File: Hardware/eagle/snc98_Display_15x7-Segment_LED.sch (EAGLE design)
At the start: 71 parts, among them M10 IRLML6402, M11 IRLML6402, M4 IRLML6402, M5 IRLML6402, M6 IRLML6402, M7 IRLML6402, M8 IRLML6402, M9 IRLML6402, X1 MICROMATCH-12, X2 MICROMATCH-14, X3 MICROMATCH-12, X4 MICROMATCH-14

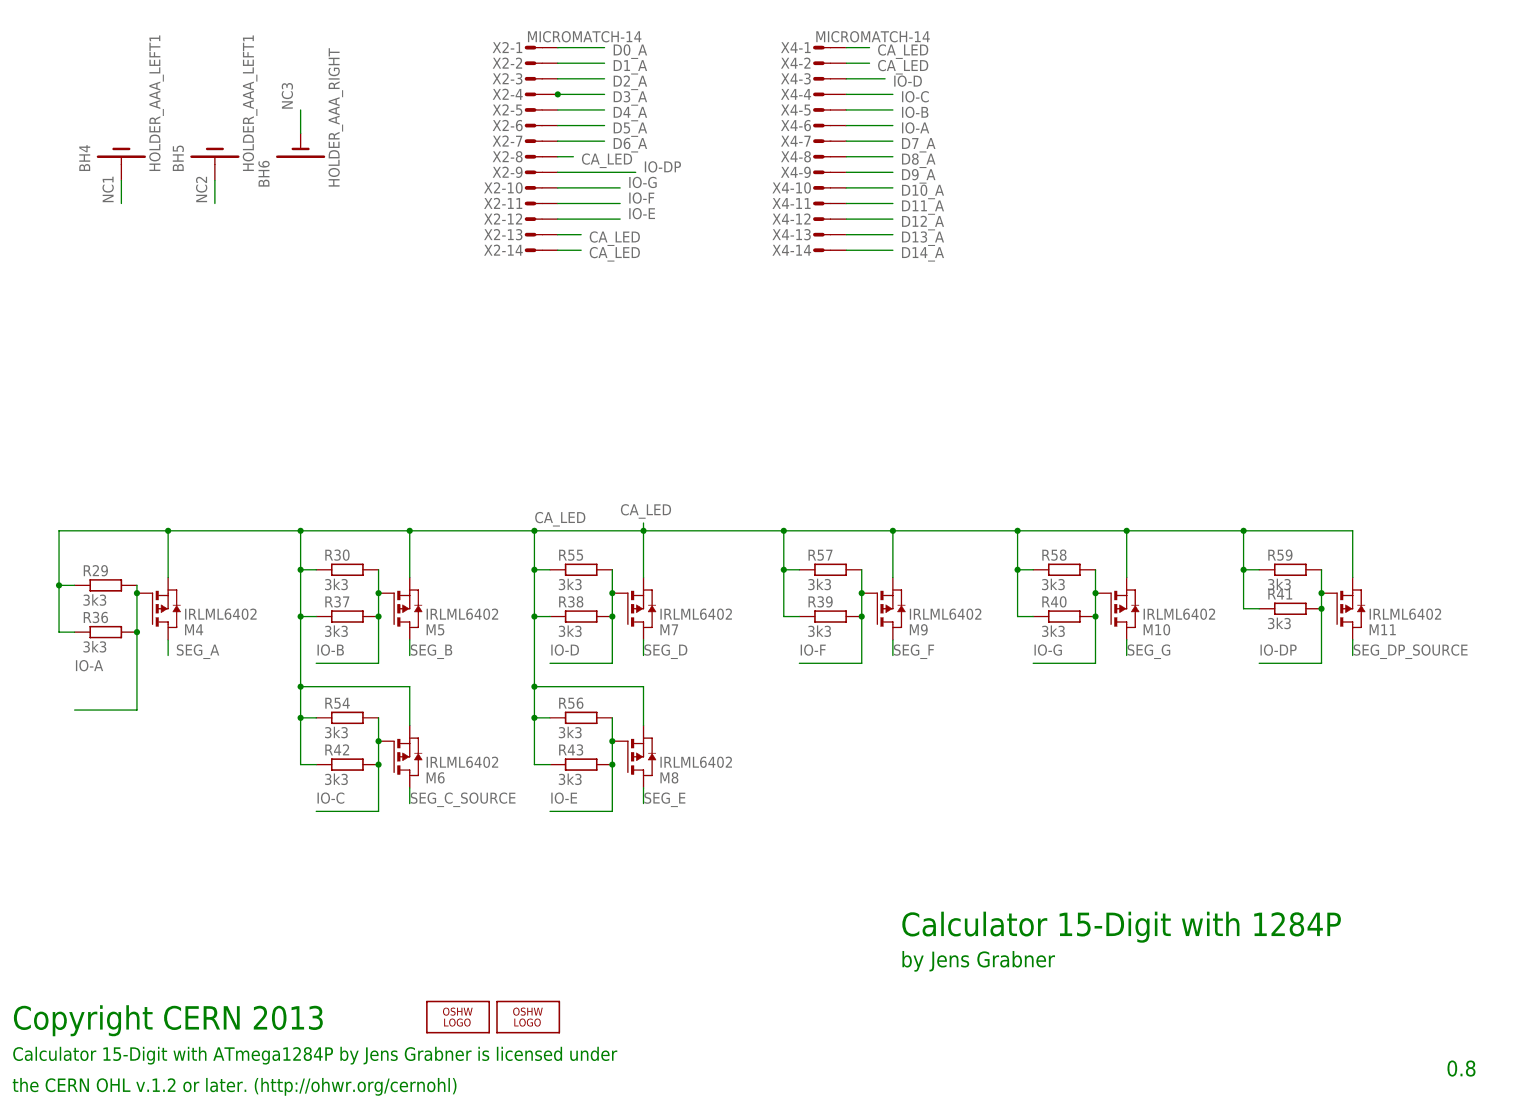
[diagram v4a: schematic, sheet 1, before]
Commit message: MR(); MS(); M+=(); Display Status
Display whe to or more switch pressed.
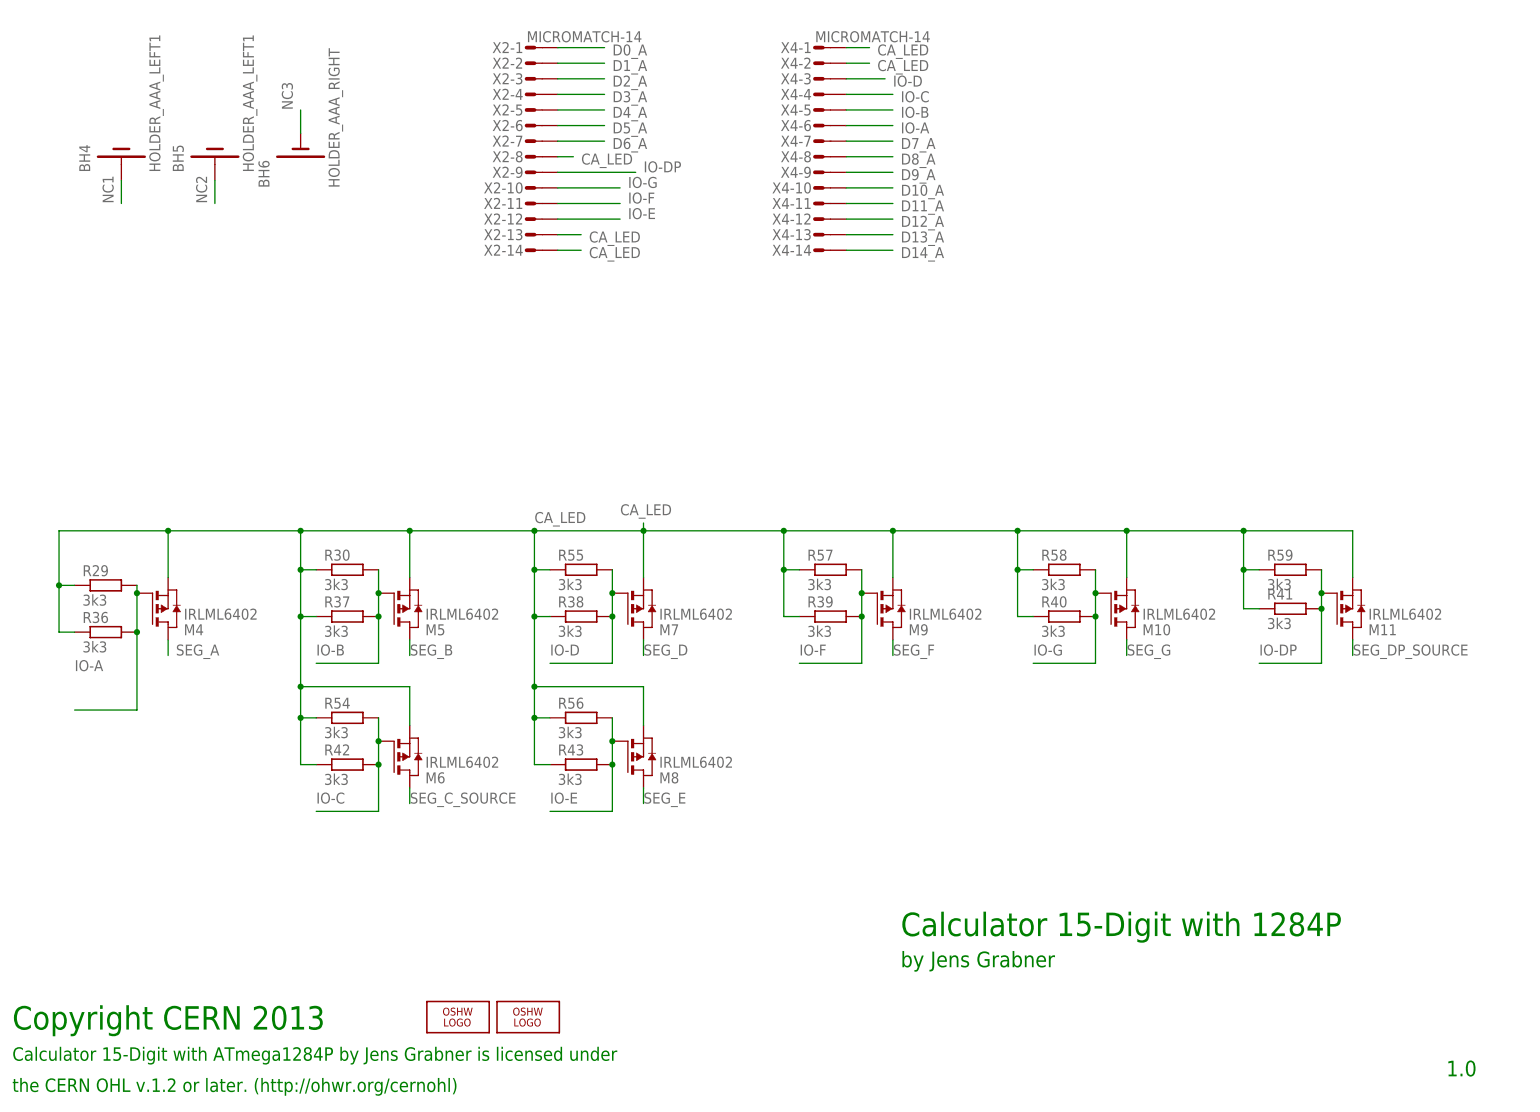
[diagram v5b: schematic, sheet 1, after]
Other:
- note added: "1.0"
- note removed: "0.8"
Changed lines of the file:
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@@
 <setting verticaltext="up"/>
 </settings>
-<grid distance="0.1" unitdist="inch" unit="inch" style="dots" multiple="1" display="no" altdistance="0.05" altunitdist="inch" altunit="inch"/>
+<grid distance="0.1" unitdist="inch" unit="inch" style="lines" multiple="1" display="no" altdistance="0.05" altunitdist="inch" altunit="inch"/>
 <layers>
 <layer number="1" name="Top" color="4" fill="1" visible="no" active="no"/>
@@
 <part name="X2" library="Con-amp-micromatch" deviceset="MICROMATCH-14" device=""/>
 <part name="X4" library="Con-amp-micromatch" deviceset="MICROMATCH-14" device=""/>
+<part name="JP2" library="adafruit" deviceset="PINHD-1X1" device=""/>
 <part name="JP1" library="adafruit" deviceset="PINHD-1X1" device=""/>
-<part name="JP2" library="adafruit" deviceset="PINHD-1X1" device=""/>
 </parts>
 <sheets>
@@
 <text x="149.86" y="30.48" size="3.81" layer="91" ratio="12">Calculator 15-Digit with 1284P</text>
 <text x="149.86" y="25.4" size="2.54" layer="91" ratio="12">by Jens Grabner</text>
-<text x="238.76" y="7.62" size="2.54" layer="91" ratio="12">0.8</text>
+<text x="238.76" y="7.62" size="2.54" layer="91" ratio="12">1.0</text>
 <text x="5.08" y="10.16" size="2.1844" layer="91" ratio="10">Calculator 15-Digit with ATmega1284P by Jens Grabner is licensed under</text>
 <text x="5.08" y="15.24" size="3.81" layer="91" ratio="12">Copyright CERN 2013</text>
@@
 <pinref part="X2" gate="-4" pin="S"/>
 <wire x1="93.98" y1="167.64" x2="101.6" y2="167.64" width="0.1524" layer="91"/>
-<junction x="93.98" y="167.64"/>
 </segment>
 </net>
@@
 <text x="-58.42" y="58.42" size="3.81" layer="91" ratio="12">Calculator 15-Digit with 1284P</text>
 <text x="-58.42" y="53.34" size="2.54" layer="91" ratio="12">by Jens Grabner</text>
-<text x="30.48" y="35.56" size="2.54" layer="91" ratio="12">0.8</text>
+<text x="30.48" y="35.56" size="2.54" layer="91" ratio="12">1.0</text>
 <text x="-203.2" y="38.1" size="2.1844" layer="91" ratio="10">Calculator 15-Digit with ATmega1284P by Jens Grabner is licensed under</text>
 <text x="-203.2" y="43.18" size="3.81" layer="91" ratio="12">Copyright CERN 2013</text>
@@
 <instance part="D26" gate="G$1" x="-3.81" y="168.91"/>
 <instance part="D27" gate="G$1" x="-3.81" y="143.51"/>
+<instance part="JP2" gate="G$1" x="17.78" y="137.16" rot="R180"/>
 <instance part="JP1" gate="G$1" x="2.54" y="132.08" rot="R180"/>
-<instance part="JP2" gate="G$1" x="17.78" y="137.16" rot="R180"/>
 </instances>
 <busses>

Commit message: New Hardware Design V0.4
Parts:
- M10, M11, M4, M5, M6, M7, M8, M9: value IRLML6402 -> IRLML2244
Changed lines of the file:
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@@
 <setting verticaltext="up"/>
 </settings>
-<grid distance="0.1" unitdist="inch" unit="inch" style="lines" multiple="1" display="no" altdistance="0.05" altunitdist="inch" altunit="inch"/>
+<grid distance="0.1" unitdist="inch" unit="inch" style="lines" multiple="1" display="yes" altdistance="0.05" altunitdist="inch" altunit="inch"/>
 <layers>
 <layer number="1" name="Top" color="4" fill="1" visible="no" active="no"/>
@@
 <part name="R18" library="rcl" deviceset="R-EU_" device="R1210" value="22"/>
 <part name="R19" library="rcl" deviceset="R-EU_" device="R1210" value="22"/>
-<part name="M4" library="IRLML6402" deviceset="IRLML6402" device=""/>
-<part name="M5" library="IRLML6402" deviceset="IRLML6402" device=""/>
-<part name="M6" library="IRLML6402" deviceset="IRLML6402" device=""/>
-<part name="M7" library="IRLML6402" deviceset="IRLML6402" device=""/>
-<part name="M8" library="IRLML6402" deviceset="IRLML6402" device=""/>
-<part name="M9" library="IRLML6402" deviceset="IRLML6402" device=""/>
-<part name="M10" library="IRLML6402" deviceset="IRLML6402" device=""/>
-<part name="M11" library="IRLML6402" deviceset="IRLML6402" device=""/>
+<part name="M4" library="IRLML6402" deviceset="IRLML6402" device="" value="IRLML2244"/>
+<part name="M5" library="IRLML6402" deviceset="IRLML6402" device="" value="IRLML2244"/>
+<part name="M6" library="IRLML6402" deviceset="IRLML6402" device="" value="IRLML2244"/>
+<part name="M7" library="IRLML6402" deviceset="IRLML6402" device="" value="IRLML2244"/>
+<part name="M8" library="IRLML6402" deviceset="IRLML6402" device="" value="IRLML2244"/>
+<part name="M9" library="IRLML6402" deviceset="IRLML6402" device="" value="IRLML2244"/>
+<part name="M10" library="IRLML6402" deviceset="IRLML6402" device="" value="IRLML2244"/>
+<part name="M11" library="IRLML6402" deviceset="IRLML6402" device="" value="IRLML2244"/>
 <part name="FRAME3" library="frames" deviceset="LETTER_L" device="" value="frame"/>
 <part name="R36" library="rcl" deviceset="R-EU_" device="R1206" value="3k3"/>
